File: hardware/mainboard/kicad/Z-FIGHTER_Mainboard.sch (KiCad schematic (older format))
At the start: 45 parts, among them IC1 Z80SIO, J1 DB9_Male_MountingHoles, J2 DB9_Male_MountingHoles, J3 USB_B, J4 Conn_02x13_Odd_Even, J5 Conn_Parallel_User, J6 Conn_PATA, J7 Conn_02x04_Odd_Even, SW1 SW_Push, SW2 SW_DIP_x03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

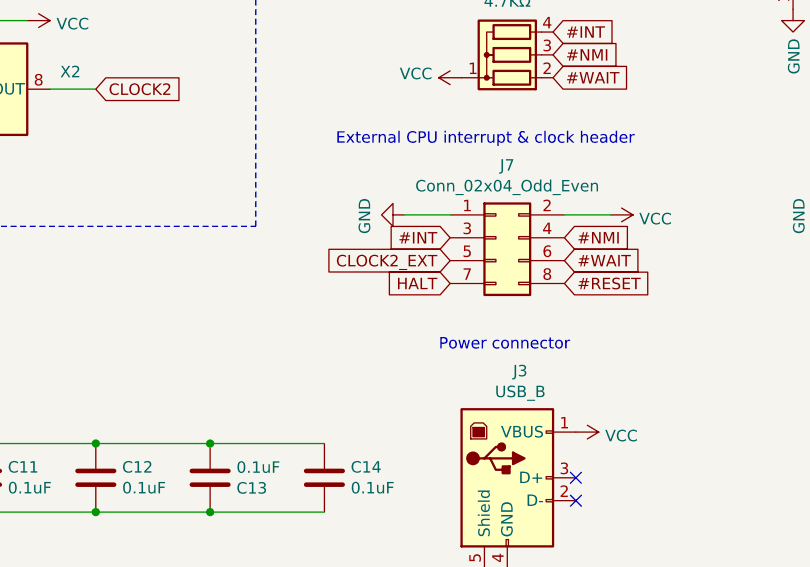
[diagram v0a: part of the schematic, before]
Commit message: Added system clock to CPU control header
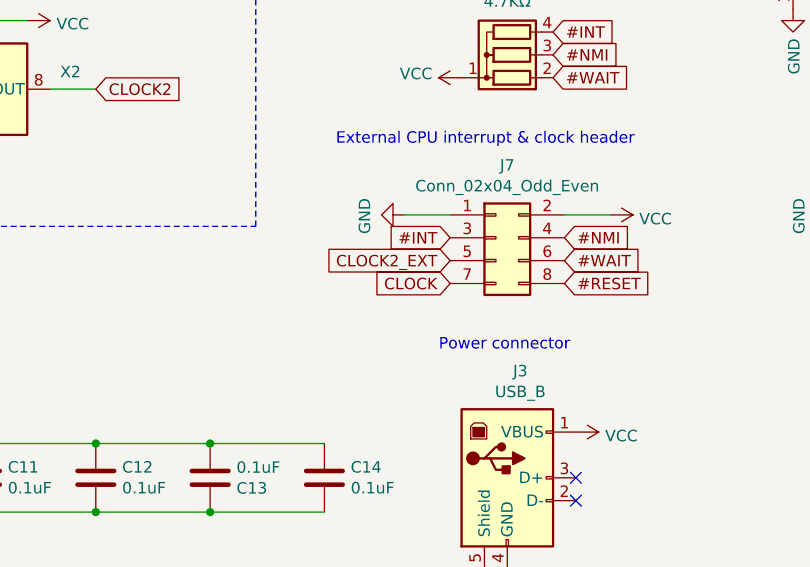
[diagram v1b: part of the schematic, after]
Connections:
- net CLOCK: now also J7.7 (Pin_7)
- net HALT: no longer J7.7 (Pin_7)
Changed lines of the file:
@@
 Text GLabel 10150 9150 2    50   Input ~ 0
 #RESET
-Text GLabel 9650 9150 0    50   Input ~ 0
-HALT
 $Comp
 L Connector_Generic:Conn_02x04_Odd_Even J7
@@
 Text GLabel 9650 8950 0    50   Input ~ 0
 #INT
+Text GLabel 9650 9150 0    50   Input ~ 0
+CLOCK
 $EndSCHEMATC

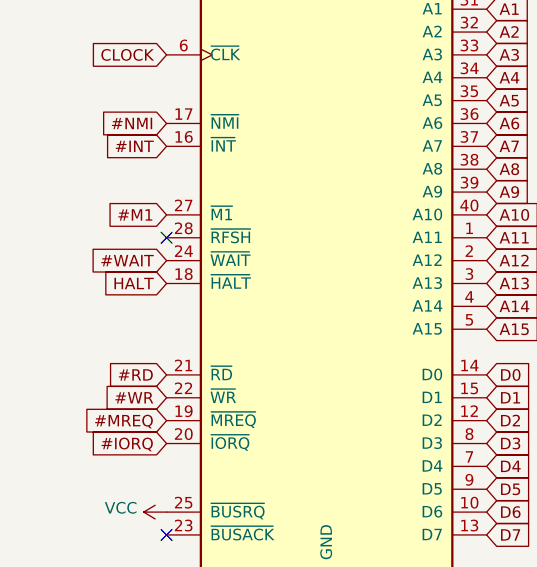
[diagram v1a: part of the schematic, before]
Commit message: nc HALT
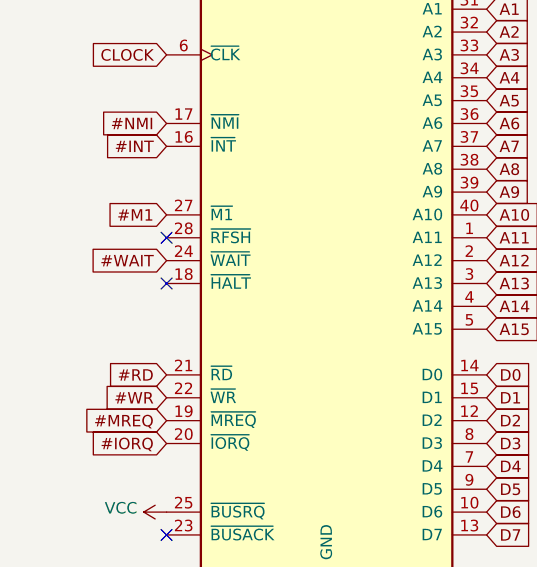
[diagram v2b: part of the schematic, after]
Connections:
- net HALT: no longer names the net of U2.18 (~HALT~)
- no-connect marks 36 -> 37
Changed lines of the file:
@@
 Text GLabel 9450 5300 0    50   Input ~ 0
 A13
-$Comp
-L CPU:Z80CPU U2
-U 1 1 5FCE363C
-P 2400 2650
-F 0 "U2" H 2400 4331 50  0000 C CNN
-F 1 "Z80CPU" H 2400 4240 50  0000 C CNN
-F 2 "Package_DIP:DIP-40_W15.24mm" H 2400 3050 50  0001 C CNN
-F 3 "www.zilog.com/manage_directlink.php?filepath=docs/z80/um0080" H 2400 3050 50  0001 C CNN
-	1    2400 2650
-	1    0    0    -1
-$EndComp
-Text GLabel 1700 2750 0    50   Input ~ 0
-HALT
 Text GLabel 10150 9150 2    50   Input ~ 0
 #RESET
@@
 Text GLabel 9650 9150 0    50   Input ~ 0
 CLOCK
+$Comp
+L CPU:Z80CPU U2
+U 1 1 5FCE363C
+P 2400 2650
+F 0 "U2" H 2400 4331 50  0000 C CNN
+F 1 "Z80CPU" H 2400 4240 50  0000 C CNN
+F 2 "Package_DIP:DIP-40_W15.24mm" H 2400 3050 50  0001 C CNN
+F 3 "www.zilog.com/manage_directlink.php?filepath=docs/z80/um0080" H 2400 3050 50  0001 C CNN
+	1    2400 2650
+	1    0    0    -1
+$EndComp
+NoConn ~ 1700 2750
 $EndSCHEMATC
